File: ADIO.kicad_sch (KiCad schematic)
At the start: 32 parts, among them U11 BTS7004-1EPP, U12 BTS7004-1EPP, U13 BTS7004-1EPP, U14 BTS7004-1EPP, U15 BTS7004-1EPP, U16 BTS7004-1EPP, U17 BTS7004-1EPP, U18 BTS7004-1EPP

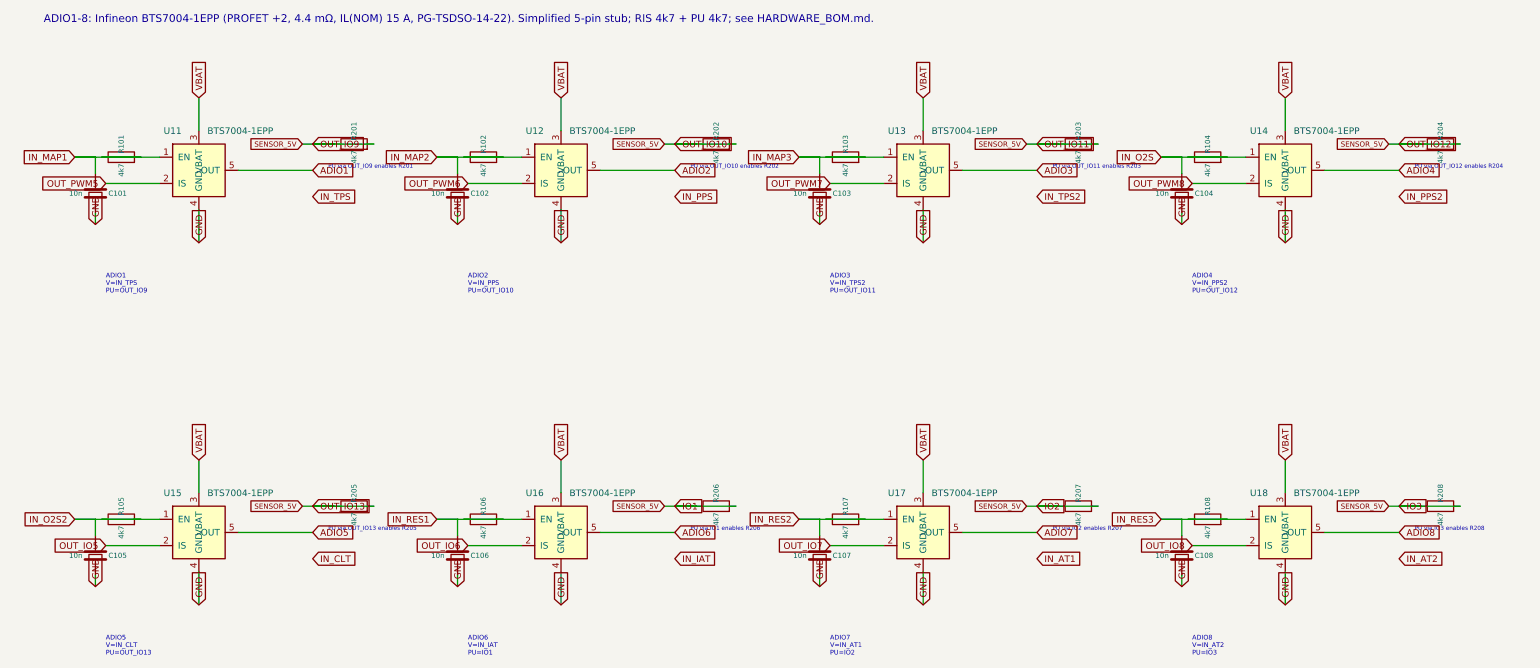
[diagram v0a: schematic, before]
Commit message: Drop even ADIO channels to 4 HP + 4 low-current outputs. (#28)
Remove ADIO2/4/6/8 drivers, sense parts, and pours, leave their SuperSeal pins no-connect, and keep the odd 8 A necks and the HP pours. Rewire J1 so schematic pin numbers match the loom, and stop the odd pull-ups from merging SENSOR_5V into IO2.

Co-authored-by: Cursor Agent <cursoragent@cursor.com>
Co-authored-by: Quintin <quintinbannink42@users.noreply.github.com>
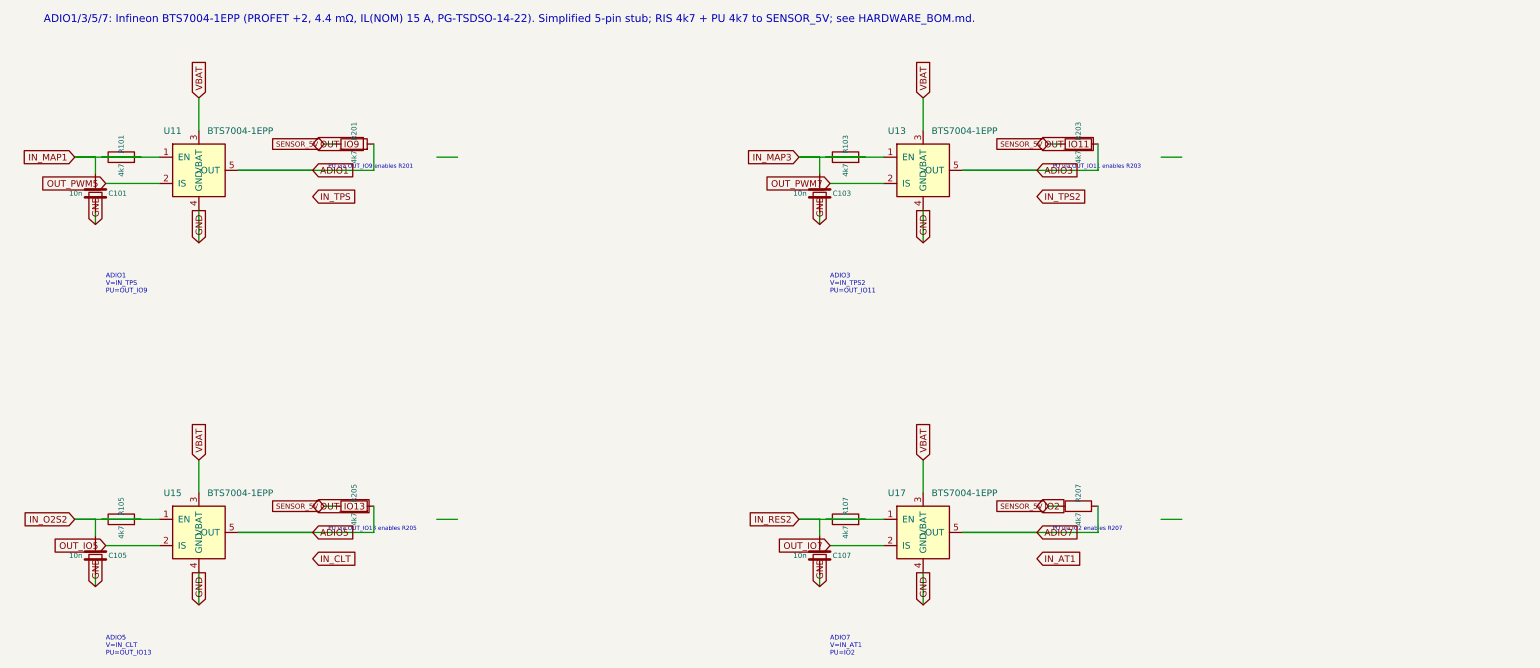
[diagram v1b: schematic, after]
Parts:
- removed C102, C104, C106, C108: 10n, Capacitor_SMD:C_0603_1608Metric, symbol Device:C
- removed R102, R104, R106, R108, R202, R204, R206, R208: 4k7, Resistor_SMD:R_0603_1608Metric, symbol Device:R
- removed U12, U14, U16, U18: BTS7004-1EPP, Package_SO:Infineon_PG-TSDSO-14-22, symbol Device:Power_Switch_PROFET_TBD
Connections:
- net ADIO1: now also R201.2
- net ADIO3: now also R203.2
- net ADIO5: now also R205.2
- net ADIO7: now also R207.2
- net IO1 renamed SENSOR_5V
- net SENSOR_5V: no longer R201.2, R203.2, R205.2, R207.2
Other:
- note added: "ADIO1/3/5/7: Infineon BTS7004-1EPP (PROFET +2, 4.4 mΩ, IL(NOM) 15 A, PG-TSDSO-14-22). Simplified 5-pin stub; RIS 4k7 + PU 4k7 to SENSOR_5V; see HARDWARE_BOM.md."
- note removed: "ADIO1-8: Infineon BTS7004-1EPP (PROFET +2, 4.4 mΩ, IL(NOM) 15 A, PG-TSDSO-14-22). Simplified 5-pin stub; RIS 4k7 + PU 4k7; see HARDWARE_BOM.md."
- note removed: "ADIO2 V=IN_PPS PU=OUT_IO10"
- note removed: "ADIO4 V=IN_PPS2 PU=OUT_IO12"
- note removed: "ADIO6 V=IN_IAT PU=IO1"
- note removed: "ADIO8 V=IN_AT2 PU=IO3"
- note removed: "PU via IO1 enables R206"
- note removed: "PU via IO3 enables R208"
- note removed: "PU via OUT_IO10 enables R202"
- note removed: "PU via OUT_IO12 enables R204"
- title: pdmrazora - ADIO x8 -> pdmrazora - ADIO x4 (8 A)
